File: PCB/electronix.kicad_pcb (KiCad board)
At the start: 2 copper layers, 95 parts, among them IC1 ICM-20602, IC2 AP9101CK6-ANTRG1, IC3 DRV8210DRLR, IC4 DRV8210DRLR, J1 USB-C 6pin, J2 PRG, M1 N20 motor, M2 N20 motor, Q1 UMH3N FHA, Q2 757-SSM6N7002KFULF, Q3 757-SSM6N7002KFULF, Q4 Phototransistor, Q5 Phototransistor, Q6 757-SSM6N7002KFULF, Q7 Phototransistor, Q8 Phototransistor, SW1 SW_DIP_x01, SW2 RESET, SW3 START, U1 MCP73213-A6SI/MF, U2 ESP32-WROOM-32, U3 LMR51420YDDRCR

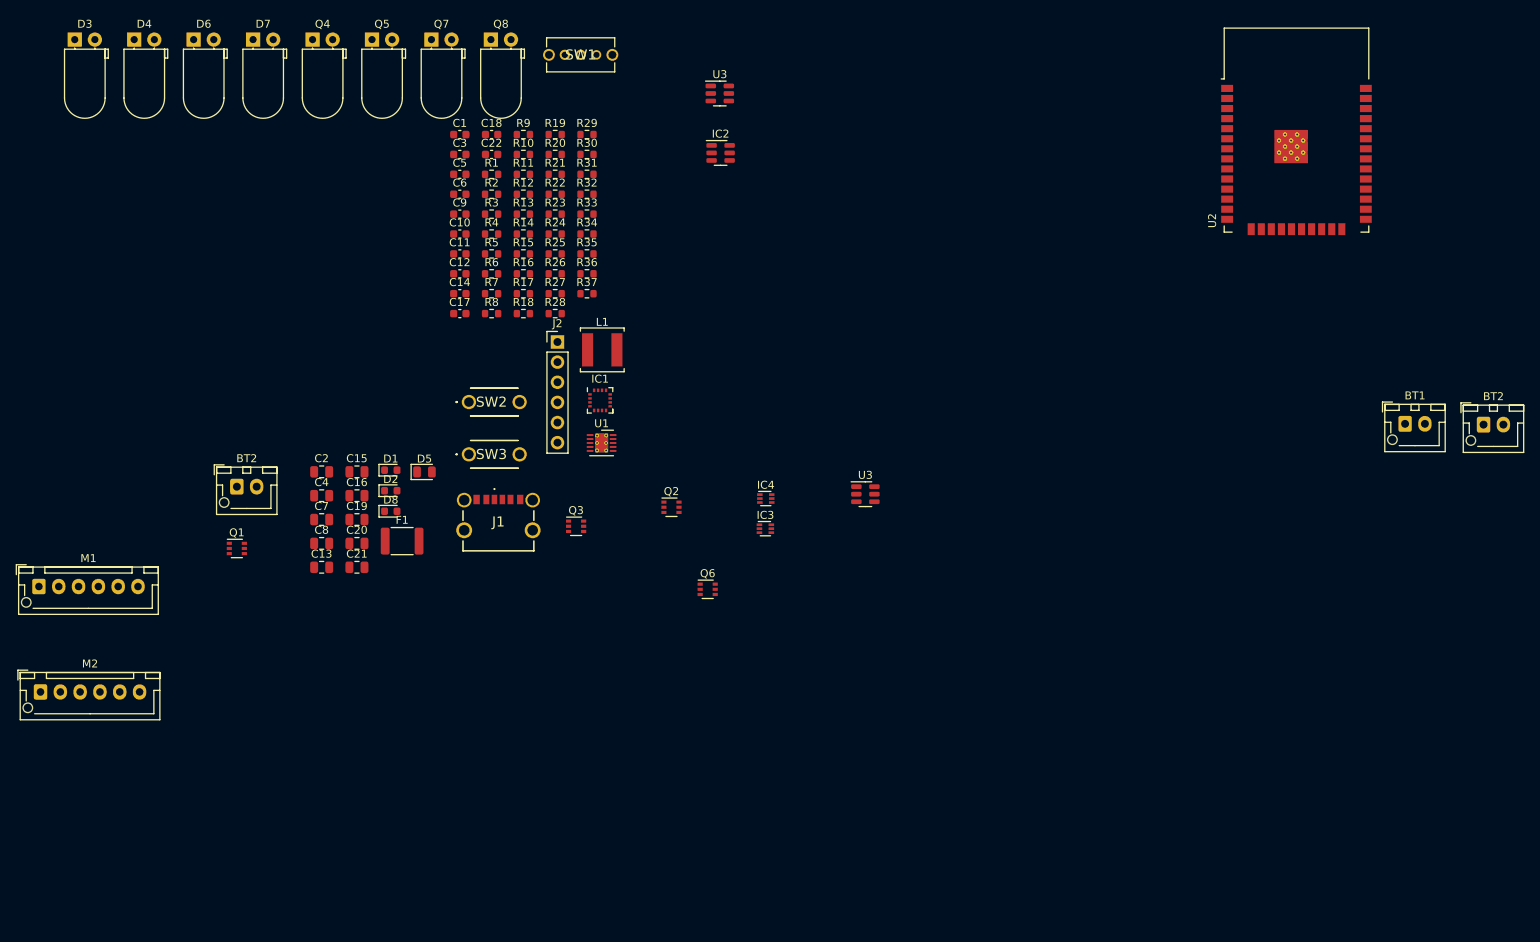
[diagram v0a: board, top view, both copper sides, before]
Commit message: Layout Add diode on prg connector remove diode on PSU to avoid driving motors from 3V3 Footprints for motors and omniwheel
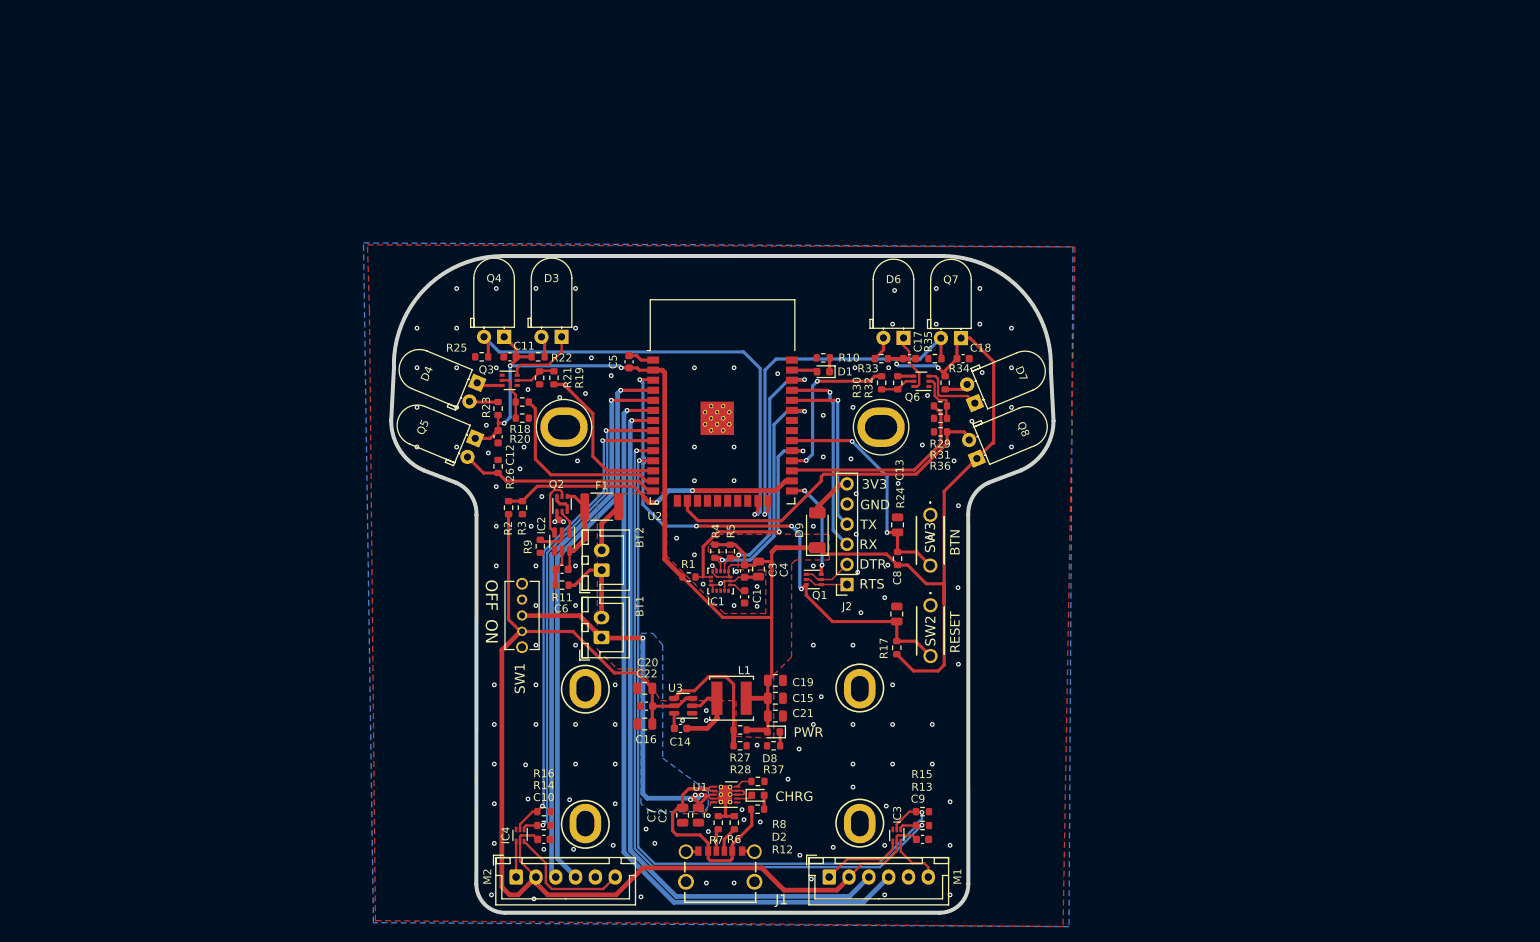
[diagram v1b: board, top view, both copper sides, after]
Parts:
- removed the BT2 at (227.1, 83.7)
- removed the BT2 at (69.8, 91.5)
- removed D5: D, Diode_SMD:D_0805_2012Metric
- removed the U3 at (130.7, 41.9)
- added BT2: li-ion, Connector_JST:JST_XH_B2B-XH-A_1x02_P2.50mm_Vertical, F.Cu at (115.8, 102.0)
- added D9: D, Diode_SMD:D_SOD-128, F.Cu at (143.0, 97.0)
- added MNT1: ~, Custom_parts:N20 encoder motor, B.Cu at (147.5, 125.5)
- added MNT2: ~, Custom_parts:N20 encoder motor, B.Cu at (114.6, 125.5)
- added MNT3: ~, Custom_parts:Ball support, B.Cu at (131.0, 84.0)
- BT1: footprint Connector_JST:JST_XH_B2B-XH-AM_1x02_P2.50mm_Vertical -> Connector_JST:JST_XH_B2B-XH-A_1x02_P2.50mm_Vertical
- IC1: footprint Package_LGA:LGA-16_3x3mm_P0.5mm -> Package_LGA:LGA-16_3x3mm_P0.5mm_LayoutBorder3x5y
- J2: footprint Connector_PinHeader_2.54mm:PinHeader_1x06_P2.54mm_Vertical -> Connector_PinSocket_2.54mm:PinSocket_1x06_P2.54mm_Vertical
- M1, M2: footprint Connector_JST:JST_XH_B6B-XH-AM_1x06_P2.50mm_Vertical -> Connector_JST:JST_XH_B6B-XH-A_1x06_P2.50mm_Vertical
- moved M1 106.2 mm to (144.5, 140.8)
- moved BT1 104.9 mm to (115.8, 110.5), turned to 90 degrees
- moved D7 102.0 mm to (162.9, 81.0), turned to 112.5 degrees
- moved C9 98.1 mm to (156.3, 136.0), turned to 180 degrees
- moved D6 97.1 mm to (153.9, 72.7), turned to 180 degrees
- moved R13 92.1 mm to (156.3, 134.2)
- moved R15 86.5 mm to (156.3, 132.5)
- moved R12 83.0 mm to (135.5, 132.2), turned to 180 degrees
- moved Q8 80.9 mm to (163.1, 88.0), turned to 112.5 degrees
- moved U2 80.1 mm to (131.0, 83.8)
- moved C10 77.1 mm to (108.5, 136.0), turned to 180 degrees
- moved Q7 76.7 mm to (161.1, 72.8), turned to 180 degrees
- moved R6 75.7 mm to (132.5, 133.9), turned to 90 degrees
- moved R14 74.7 mm to (108.5, 134.2)
- moved C8 73.1 mm to (153.0, 107.6), turned to 90 degrees
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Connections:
- net Net-(Q1B-C1) renamed /IO0
- IC1 pad 2: /SDA -> /SCL
- IC1 pad 3: /SCL -> /SDA
- J2 pad 5: +3V3 -> GND
- J2 pad 6: GND -> Net-(D9-A)
- Q1 pad 3: Net-(Q1A-C1) -> /EN
- R4 pad 2: /SCL -> /SDA
- R5 pad 2: /SDA -> /SCL
- SW1 pad 1: VCC -> unconnected-(SW1-Pad1)
- SW1 pad 3: unconnected-(SW1-Pad3) -> VCC
- U2 pad 12: /prox_in_r -> /prox_in_l
- U2 pad 14: /prox_out_r -> /prox_out_l
- U2 pad 16: /prox_out_l -> /prox_out_r
- U2 pad 23: /prox_out_fr -> /prox_out_fl
- U2 pad 24: /prox_out_fl -> /prox_out_fr
- U2 pad 28: /prox_in_l -> /prox_in_r
- U2 pad 3: Net-(Q1A-C1) -> /EN
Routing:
- net +3V3: track 0.00 -> 220.2 mm, vias 0 -> 5
- net VCC: track 0.00 -> 148.4 mm
- net /M1c1: track 0.00 -> 96.5 mm, vias 0 -> 1
- net /M1in2: track 0.00 -> 95.2 mm, vias 0 -> 2
- net /M1in1: track 0.00 -> 94.8 mm, vias 0 -> 2
- net /M1c2: track 0.00 -> 90.5 mm, vias 0 -> 1
- net /M2c1: track 0.00 -> 69.8 mm, vias 0 -> 1
- net /M2c2: track 0.00 -> 68.8 mm, vias 0 -> 1
- net /EN: track 0.00 -> 68.6 mm, vias 0 -> 4
- net /M2in1: track 0.00 -> 61.9 mm, vias 0 -> 2
- net /M2in2: track 0.00 -> 60.2 mm, vias 0 -> 2
- net /prox_out_fl: track 0.00 -> 60.0 mm, vias 0 -> 1
- net +BATT: track 0.00 -> 53.0 mm, vias 0 -> 4
- net /prox_out_fr: track 0.00 -> 46.6 mm, vias 0 -> 1
- net /prox_out_r: track 0.00 -> 43.3 mm
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- added copper zone on F.Cu, net +3V3
- added copper zone on B.Cu, net +BATT
- added copper zone on F.Cu, net +BATT
- added copper zone on B.Cu, net GND
- added copper zone on F.Cu, net GND
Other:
- board outline added: 83.6 x 82.9 mm
- board text added: "3V3"
- board text added: "BTN"
- board text added: "CHRG"
- board text added: "DTR"
- board text added: "GND"
- board text added: "OFF"
- board text added: "ON"
- board text added: "PWR"
- board text added: "RESET"
- board text added: "RTS"
- board text added: "RX"
- board text added: "TX"

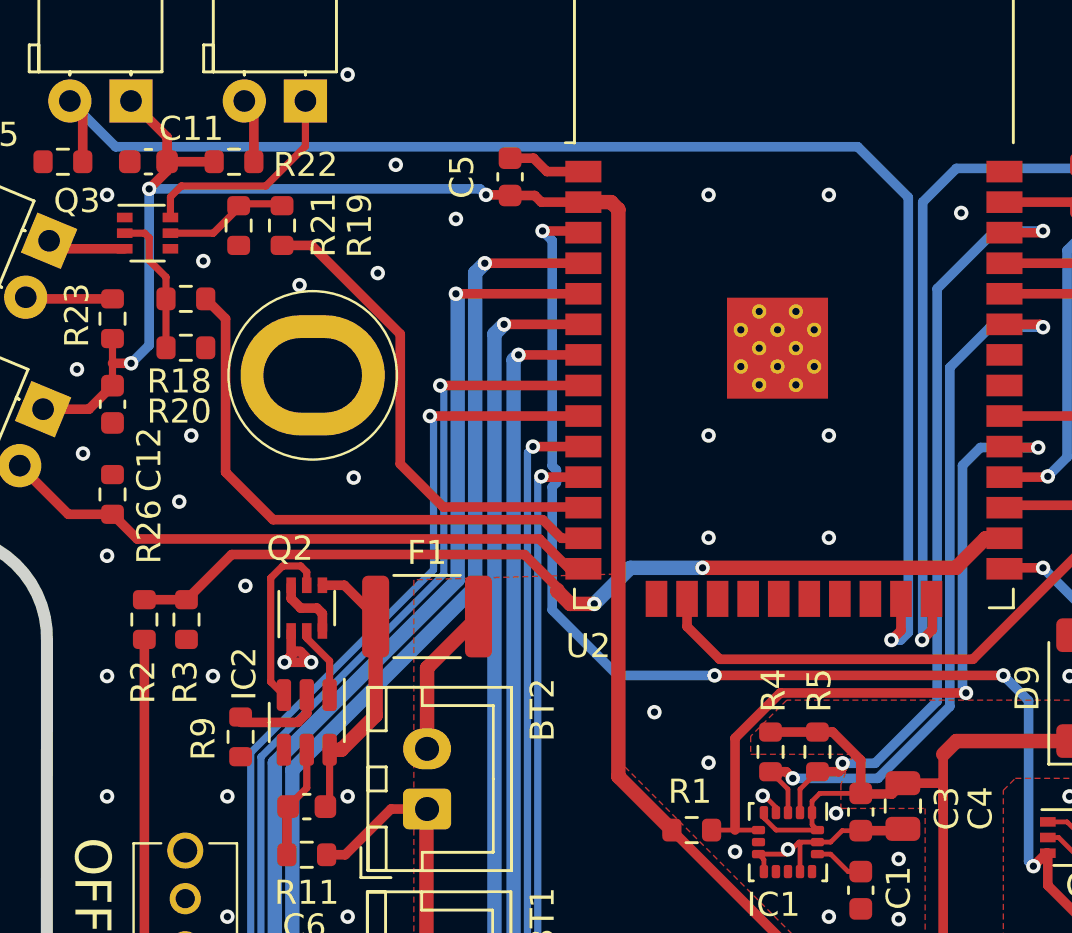
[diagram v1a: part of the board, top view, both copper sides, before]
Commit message: add bigger ESP32 bypass
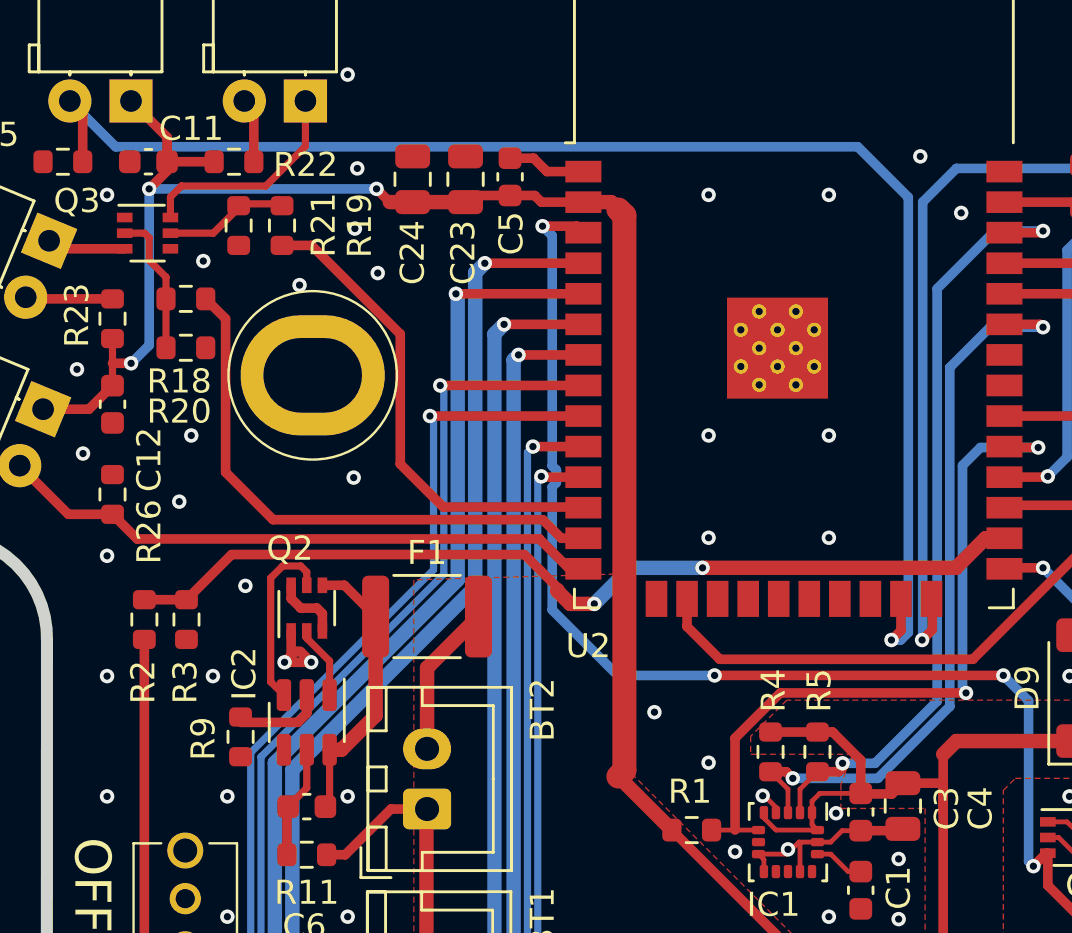
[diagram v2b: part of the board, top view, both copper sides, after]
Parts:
- added C23: 4u7/50V, Capacitor_SMD:C_0805_2012Metric, F.Cu at (117.4, 75.8)
- added C24: 4u7/50V, Capacitor_SMD:C_0805_2012Metric, F.Cu at (115.2, 75.8)
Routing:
- net GND: vias 145 -> 146

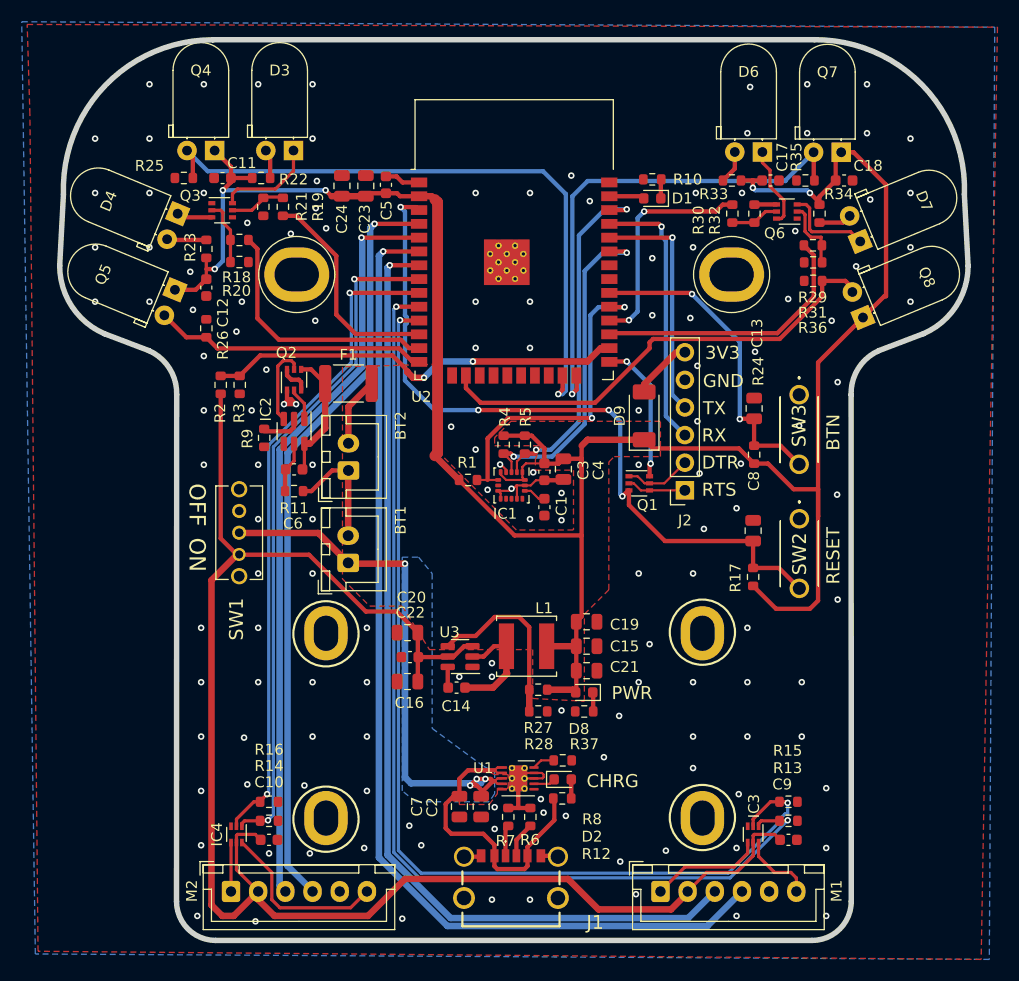
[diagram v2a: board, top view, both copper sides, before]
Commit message: Layout edits Power line hardening Fabrication outputs
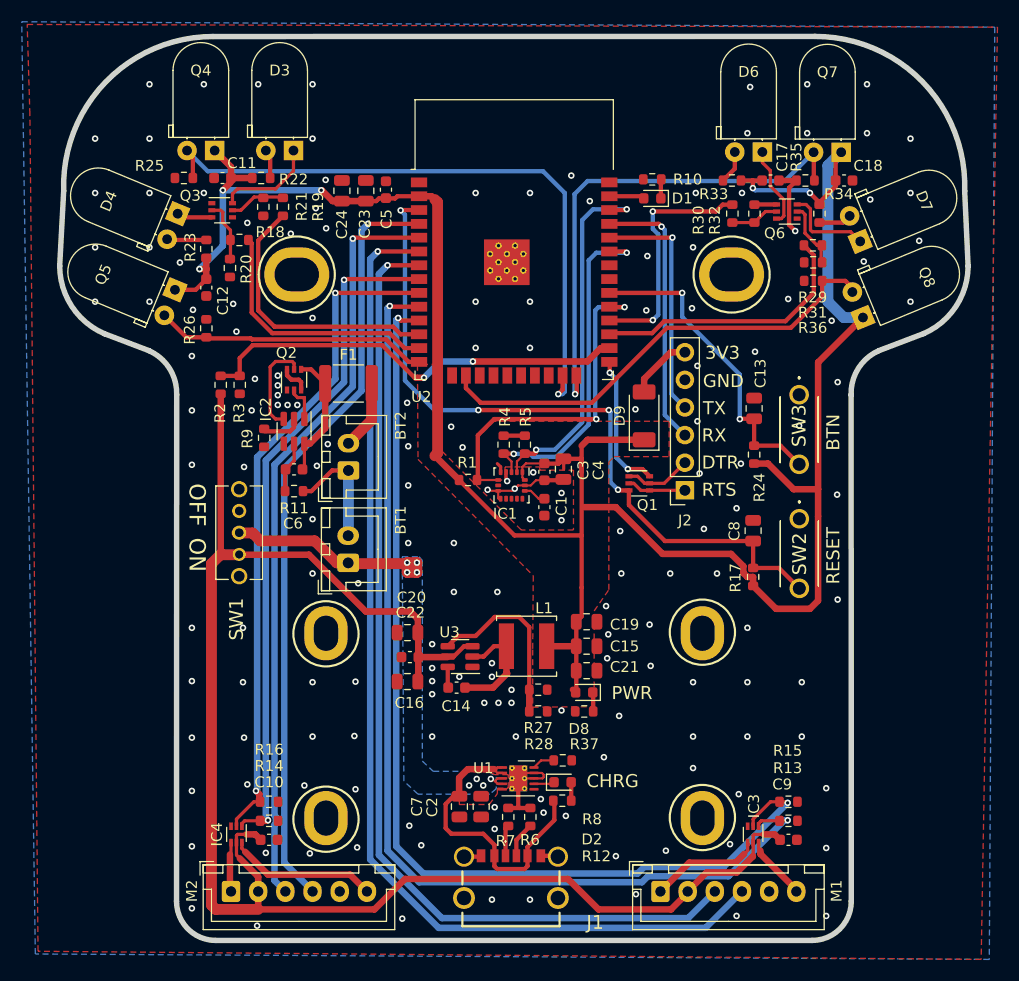
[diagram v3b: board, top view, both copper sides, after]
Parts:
- moved R20 1.03 mm to (104.9, 83.4), turned to -90 degrees
- moved C23 0.45 mm to (117.4, 76.3)
- moved C24 0.45 mm to (115.2, 76.3)
- moved C5 0.45 mm to (119.2, 76.2)
- moved D2 0.26 mm to (135.5, 130.7)
- moved R12 0.21 mm to (135.5, 132.4)
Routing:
- net +BATT: track 53.0 -> 21.8 mm, vias 4 -> 8
- net /prox_in_l: track 20.2 -> 25.3 mm
- net +3V3: track 220.7 -> 218.2 mm
- net /M2n: track 16.1 -> 13.7 mm
- net GND: track 32.0 -> 30.2 mm, vias 146 -> 170
- net /v_sense: track 38.5 -> 40.2 mm
- net /M1c1: track 96.5 -> 98.2 mm
- net /M1in1: track 94.8 -> 96.3 mm
- net Net-(IC2-CO): track 7.45 -> 8.78 mm
- net /IMU_int: track 30.5 -> 31.8 mm
- net /M1c2: track 90.5 -> 91.8 mm
- net /prox_in_r: track 20.8 -> 22.0 mm
- net /EN: track 68.9 -> 67.7 mm
- net /M1n: track 6.82 -> 5.79 mm
- net /SCL: track 32.5 -> 33.3 mm
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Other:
- board size 83.6 x 82.9 mm -> 83.6 x 83.2 mm
- board text added: "JLCJLCJLCJLC"
